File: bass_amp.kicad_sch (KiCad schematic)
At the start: 20 parts, among them J1 AudioJack3, J2 PICKUP_SIGNAL, J3 PICKUP_GND, J4 PWR, J5 GND, Q1 BC547, Q2 BC547, SW1 SW_Push_DPDT

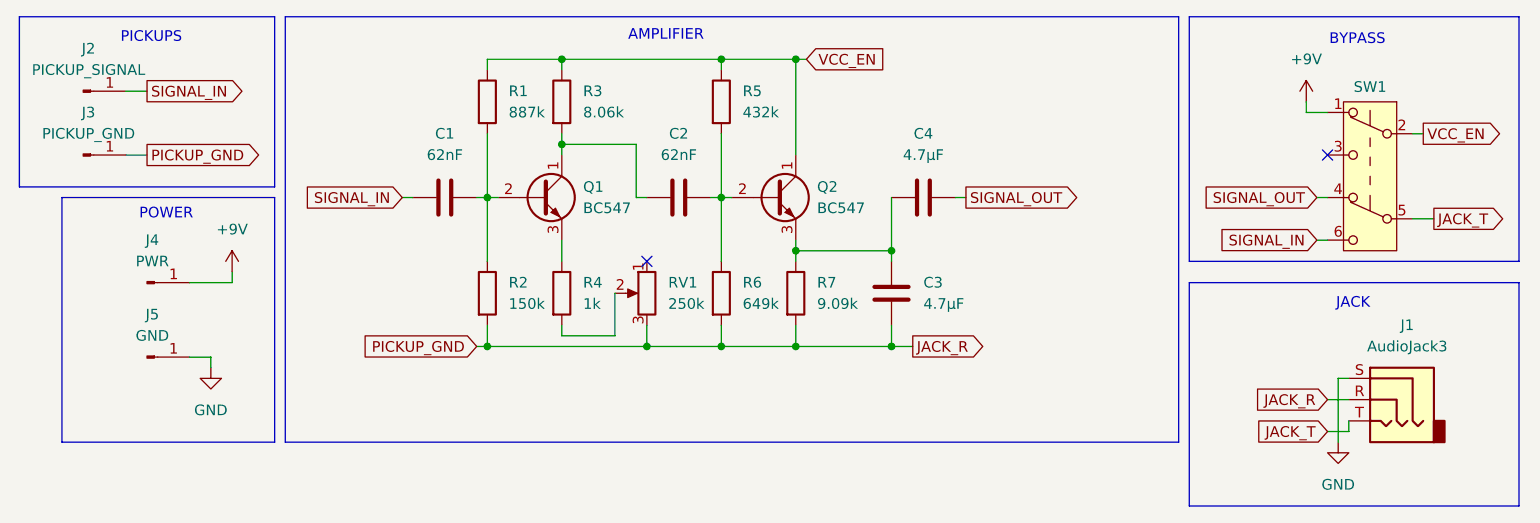
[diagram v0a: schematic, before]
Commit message: Fix GND connections and rewire the board's GND traces
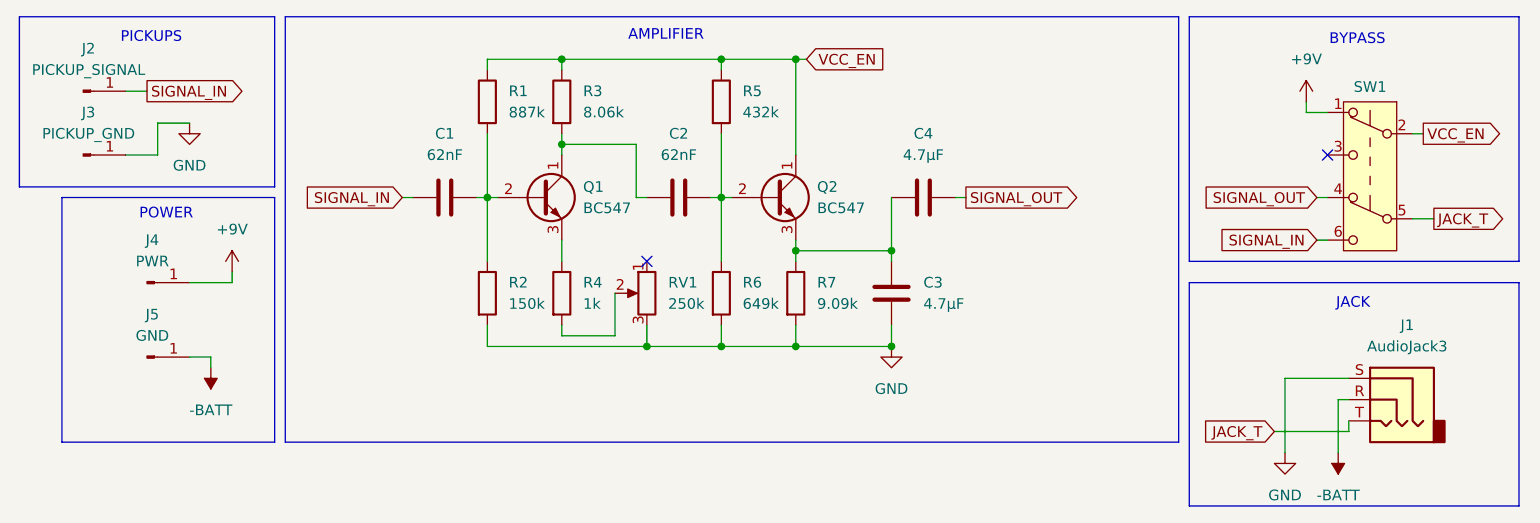
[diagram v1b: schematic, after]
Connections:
- net GND: now also C3.2, J3.1 (Pin_1), R2.2, R6.2, R7.2, RV1.3; no longer J5.1 (Pin_1)
- removed net JACK_R: C3.2, J1.R, J3.1 (Pin_1), R2.2, R6.2, R7.2, RV1.3
- new net -BATT: J1.R, J5.1 (Pin_1)
